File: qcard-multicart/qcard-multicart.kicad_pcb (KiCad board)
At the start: 2 copper layers, 55 x 54.5 mm, 14 parts, among them J1 Conn_02x18_Top_Bottom, SW1 774-1954MST, U1 MX29LV640EBTI-70G, U2 MIC5365-3.3YD5

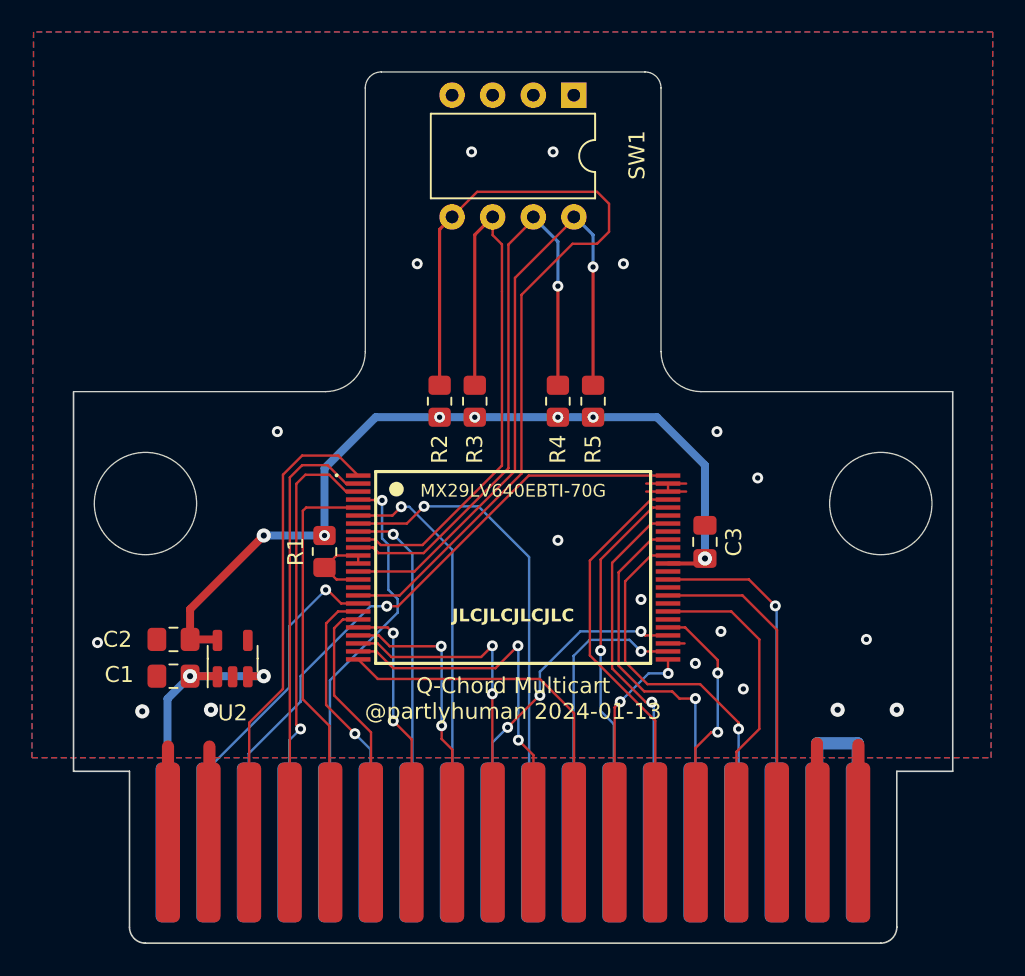
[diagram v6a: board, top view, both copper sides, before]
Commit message: Space out components for easier hand soldering
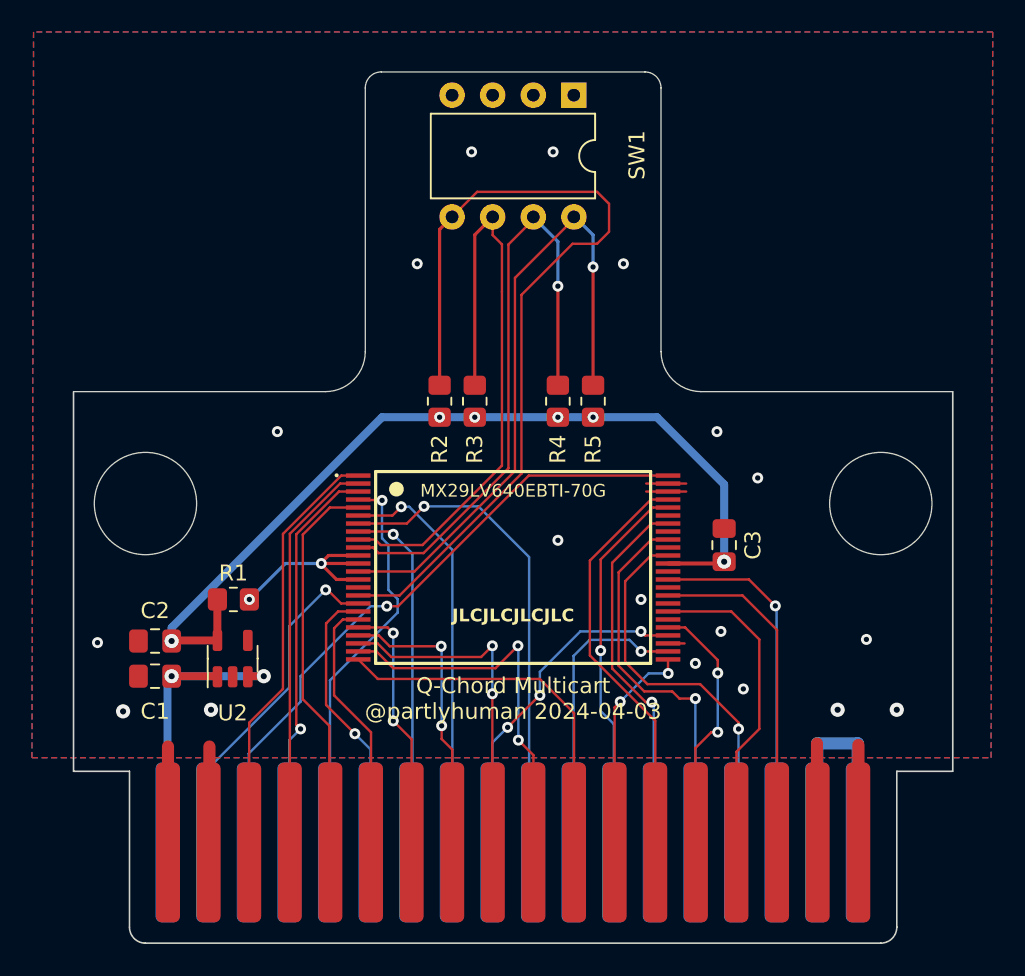
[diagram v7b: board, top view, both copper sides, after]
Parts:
- removed REF**: MountingHole_6.4mm_M6, MountingHole:MountingHole_6.4mm_M6
- added H2: MountingHole_6.4mm_M6, MountingHole:MountingHole_6.4mm_M6, F.Cu at (120.0, 54.0)
- moved R1 6.44 mm to (79.5, 60.0), turned to 0 degrees
- moved C3 1.22 mm to (110.2, 56.6)
- moved C2 1.16 mm to (74.6, 62.6)
- moved C1 1.15 mm to (74.6, 64.8)
- renumbered REF** to H1
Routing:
- net Net-(U1-WE#): track 5.34 -> 13.0 mm, vias 0 -> 2
- net +3.3V: track 52.8 -> 56.5 mm, vias 7 -> 6
- net /A16: track 29.9 -> 26.7 mm
- net /A15: track 28.2 -> 25.2 mm
- net /A14: track 27.7 -> 25.0 mm
- net +5V: track 18.3 -> 20.2 mm
- net /A12: track 25.3 -> 24.4 mm
